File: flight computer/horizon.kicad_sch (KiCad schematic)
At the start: 44 parts, among them J2 Conn_02x03_Counter_Clockwise, J7 Conn_02x03_Counter_Clockwise, J8 Conn_02x03_Counter_Clockwise, SW1 CK_KMS2xxG, U1 MMCU, U2 MKL02Z32VFG4, Y1 32 kHZ

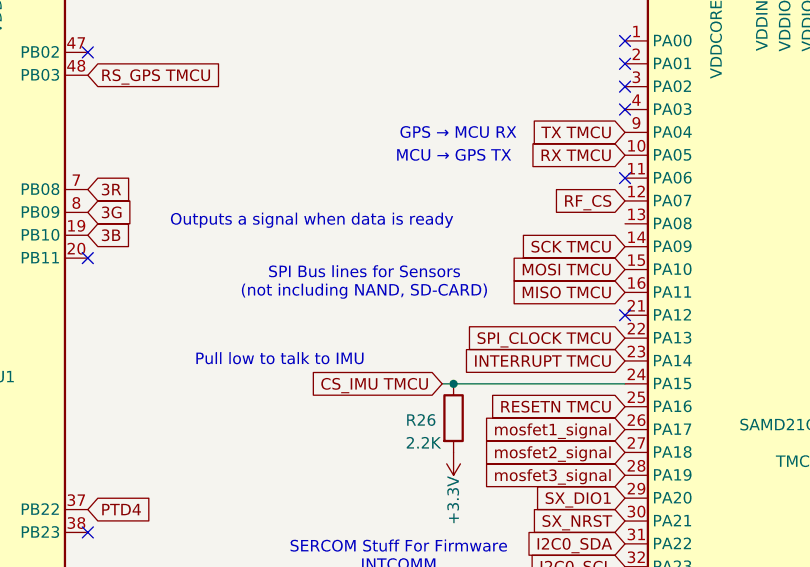
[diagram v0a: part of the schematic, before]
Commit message: swap spi lines on tmcu
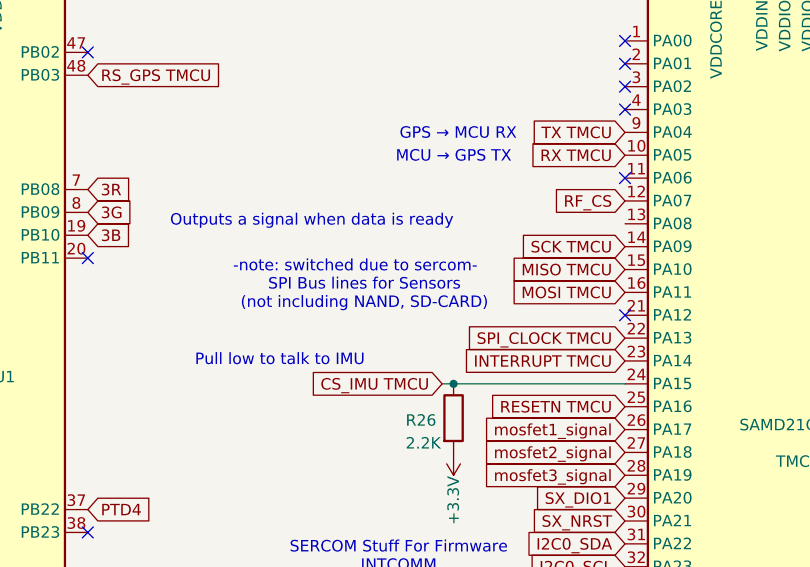
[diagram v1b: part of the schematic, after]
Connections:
- net MISO TMCU: now also SAMD21G18A-AU2.15 (PA10); no longer SAMD21G18A-AU2.16 (PA11)
- net MOSI TMCU: now also SAMD21G18A-AU2.16 (PA11); no longer SAMD21G18A-AU2.15 (PA10)
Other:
- note added: "-note: switched due to sercom-"
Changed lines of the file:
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@@
+		)
+	)
+	(text "-note: switched due to sercom-"
+		(exclude_from_sim no)
+		(at 97.028 69.596 0)
+		(effects
+			(font
+				(size 1.27 1.27)
+			)
 		)
 	)
@@
 	(text "SPI Bus lines for Sensors \n(not including NAND, SD-CARD)"
 		(exclude_from_sim no)
-		(at 98.044 71.374 0)
+		(at 98.044 72.644 0)
 		(effects
 			(font
@@
 	(global_label "MOSI TMCU"
 		(shape input)
+		(at 127 72.39 180)
+		(fields_autoplaced yes)
+		(effects
+			(font
+				(size 1.27 1.27)
+			)
+			(justify right)
+		)
+		(property "Intersheetrefs" "${INTERSHEET_REFS}"
+			(at 113.4315 72.39 0)
+			(effects
+				(font
+					(size 1.27 1.27)
+				)
+				(justify right)
+				(hide yes)
+			)
+		)
+	)
+	(global_label "CAM_TX"
+		(shape input)
+		(at 232.41 30.48 180)
+		(fields_autoplaced yes)
+		(effects
+			(font
+				(size 1.27 1.27)
+			)
+			(justify right)
+		)
+		(property "Intersheetrefs" "${INTERSHEET_REFS}"
+			(at 222.4701 30.48 0)
+			(effects
+				(font
+					(size 1.27 1.27)
+				)
+				(justify right)
+				(hide yes)
+			)
+		)
+	)
+	(global_label "2G"
+		(shape input)
+		(at 162.56 67.31 0)
+		(fields_autoplaced yes)
+		(effects
+			(font
+				(size 1.27 1.27)
+			)
+			(justify left)
+		)
+		(property "Intersheetrefs" "${INTERSHEET_REFS}"
+			(at 168.0247 67.31 0)
+			(effects
+				(font
+					(size 1.27 1.27)
+				)
+				(justify left)
+				(hide yes)
+			)
+		)
+	)
+	(global_label "SCK TMCU"
+		(shape input)
+		(at 127 67.31 180)
+		(fields_autoplaced yes)
+		(effects
+			(font
+				(size 1.27 1.27)
+			)
+			(justify right)
+		)
+		(property "Intersheetrefs" "${INTERSHEET_REFS}"
+			(at 114.2782 67.31 0)
+			(effects
+				(font
+					(size 1.27 1.27)
+				)
+				(justify right)
+				(hide yes)
+			)
+		)
+	)
+	(global_label "D+ DMCU-2"
+		(shape input)
+		(at 118.11 107.95 180)
+		(fields_autoplaced yes)
+		(effects
+			(font
+				(size 1.27 1.27)
+			)
+			(justify right)
+		)
+		(property "Intersheetrefs" "${INTERSHEET_REFS}"
+			(at 103.211 107.95 0)
+			(effects
+				(font
+					(size 1.27 1.27)
+				)
+				(justify right)
+				(hide yes)
+			)
+		)
+	)
+	(global_label "TX TMCU"
+		(shape input)
+		(at 127 54.61 180)
+		(fields_autoplaced yes)
+		(effects
+			(font
+				(size 1.27 1.27)
+			)
+			(justify right)
+		)
+		(property "Intersheetrefs" "${INTERSHEET_REFS}"
+			(at 115.8506 54.61 0)
+			(effects
+				(font
+					(size 1.27 1.27)
+				)
+				(justify right)
+				(hide yes)
+			)
+		)
+	)
+	(global_label "PTA2"
+		(shape input)
+		(at 290.83 106.68 0)
+		(fields_autoplaced yes)
+		(effects
+			(font
+				(size 1.27 1.27)
+			)
+			(justify left)
+		)
+		(property "Intersheetrefs" "${INTERSHEET_REFS}"
+			(at 298.3509 106.68 0)
+			(effects
+				(font
+					(size 1.27 1.27)
+				)
+				(justify left)
+				(hide yes)
+			)
+		)
+	)
+	(global_label "MISO TMCU"
+		(shape input)
 		(at 127 69.85 180)
 		(fields_autoplaced yes)
@@
 			(effects
 				(font
-					(size 1.27 1.27)
-				)
-				(justify right)
-				(hide yes)
-			)
-		)
-	)
-	(global_label "CAM_TX"
-		(shape input)
-		(at 232.41 30.48 180)
-		(fields_autoplaced yes)
-		(effects
-			(font
-				(size 1.27 1.27)
-			)
-			(justify right)
-		)
-		(property "Intersheetrefs" "${INTERSHEET_REFS}"
-			(at 222.4701 30.48 0)
-			(effects
-				(font
-					(size 1.27 1.27)
-				)
-				(justify right)
-				(hide yes)
-			)
-		)
-	)
-	(global_label "2G"
-		(shape input)
-		(at 162.56 67.31 0)
-		(fields_autoplaced yes)
-		(effects
-			(font
-				(size 1.27 1.27)
-			)
-			(justify left)
-		)
-		(property "Intersheetrefs" "${INTERSHEET_REFS}"
-			(at 168.0247 67.31 0)
-			(effects
-				(font
-					(size 1.27 1.27)
-				)
-				(justify left)
-				(hide yes)
-			)
-		)
-	)
-	(global_label "SCK TMCU"
-		(shape input)
-		(at 127 67.31 180)
-		(fields_autoplaced yes)
-		(effects
-			(font
-				(size 1.27 1.27)
-			)
-			(justify right)
-		)
-		(property "Intersheetrefs" "${INTERSHEET_REFS}"
-			(at 114.2782 67.31 0)
-			(effects
-				(font
-					(size 1.27 1.27)
-				)
-				(justify right)
-				(hide yes)
-			)
-		)
-	)
-	(global_label "D+ DMCU-2"
-		(shape input)
-		(at 118.11 107.95 180)
-		(fields_autoplaced yes)
-		(effects
-			(font
-				(size 1.27 1.27)
-			)
-			(justify right)
-		)
-		(property "Intersheetrefs" "${INTERSHEET_REFS}"
-			(at 103.211 107.95 0)
-			(effects
-				(font
-					(size 1.27 1.27)
-				)
-				(justify right)
-				(hide yes)
-			)
-		)
-	)
-	(global_label "TX TMCU"
-		(shape input)
-		(at 127 54.61 180)
-		(fields_autoplaced yes)
-		(effects
-			(font
-				(size 1.27 1.27)
-			)
-			(justify right)
-		)
-		(property "Intersheetrefs" "${INTERSHEET_REFS}"
-			(at 115.8506 54.61 0)
-			(effects
-				(font
-					(size 1.27 1.27)
-				)
-				(justify right)
-				(hide yes)
-			)
-		)
-	)
-	(global_label "PTA2"
-		(shape input)
-		(at 290.83 106.68 0)
-		(fields_autoplaced yes)
-		(effects
-			(font
-				(size 1.27 1.27)
-			)
-			(justify left)
-		)
-		(property "Intersheetrefs" "${INTERSHEET_REFS}"
-			(at 298.3509 106.68 0)
-			(effects
-				(font
-					(size 1.27 1.27)
-				)
-				(justify left)
-				(hide yes)
-			)
-		)
-	)
-	(global_label "MISO TMCU"
-		(shape input)
-		(at 127 72.39 180)
-		(fields_autoplaced yes)
-		(effects
-			(font
-				(size 1.27 1.27)
-			)
-			(justify right)
-		)
-		(property "Intersheetrefs" "${INTERSHEET_REFS}"
-			(at 113.4315 72.39 0)
-			(effects
-				(font

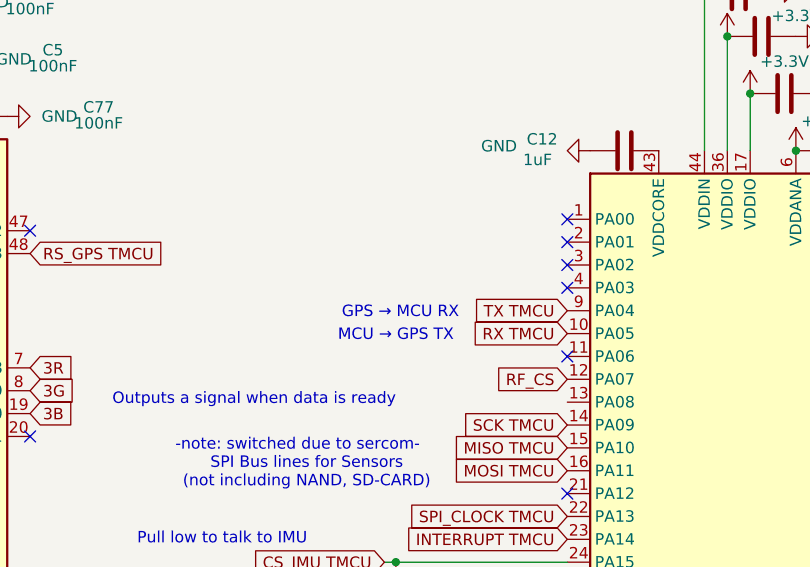
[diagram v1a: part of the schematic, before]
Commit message: note: referenced to vddana
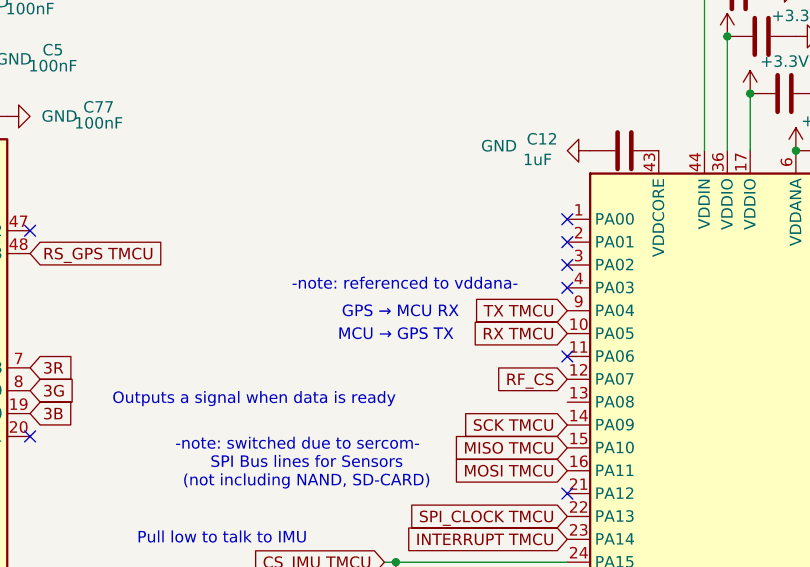
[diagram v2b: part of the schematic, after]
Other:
- note added: "-note: referenced to vddana-"
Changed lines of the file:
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@@
+		)
+	)
+	(text "-note: referenced to vddana-"
+		(exclude_from_sim no)
+		(at 108.966 51.816 0)
+		(effects
+			(font
+				(size 1.27 1.27)
+			)
 		)
 	)

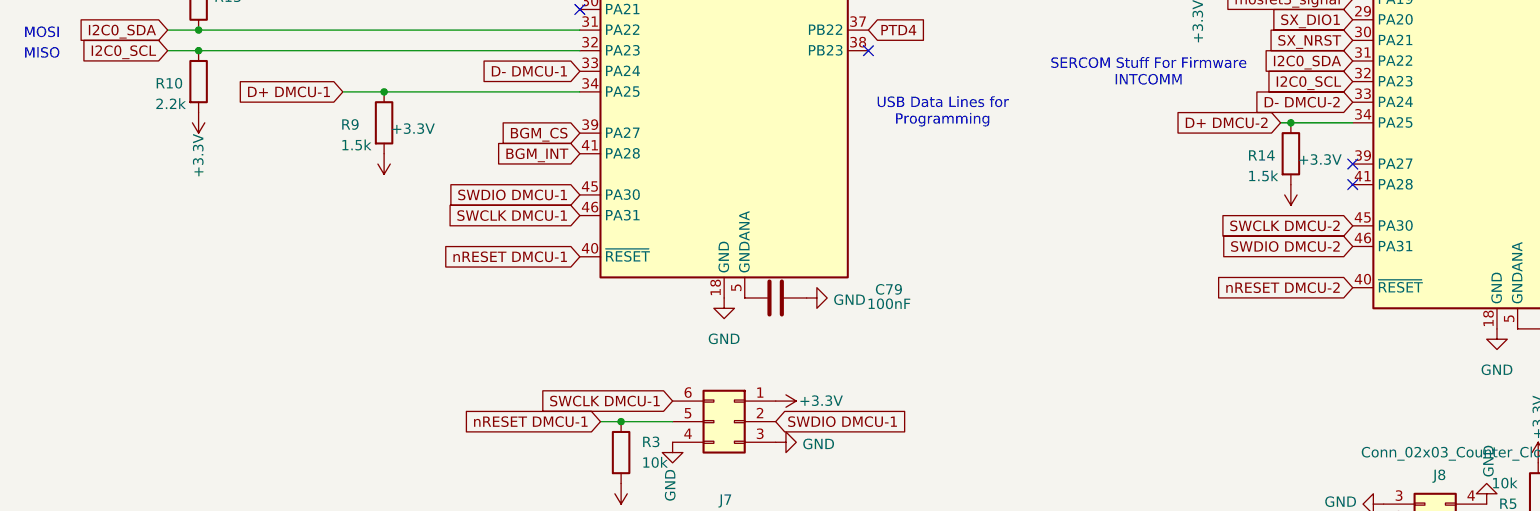
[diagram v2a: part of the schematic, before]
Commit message: swapping swd on nmcu
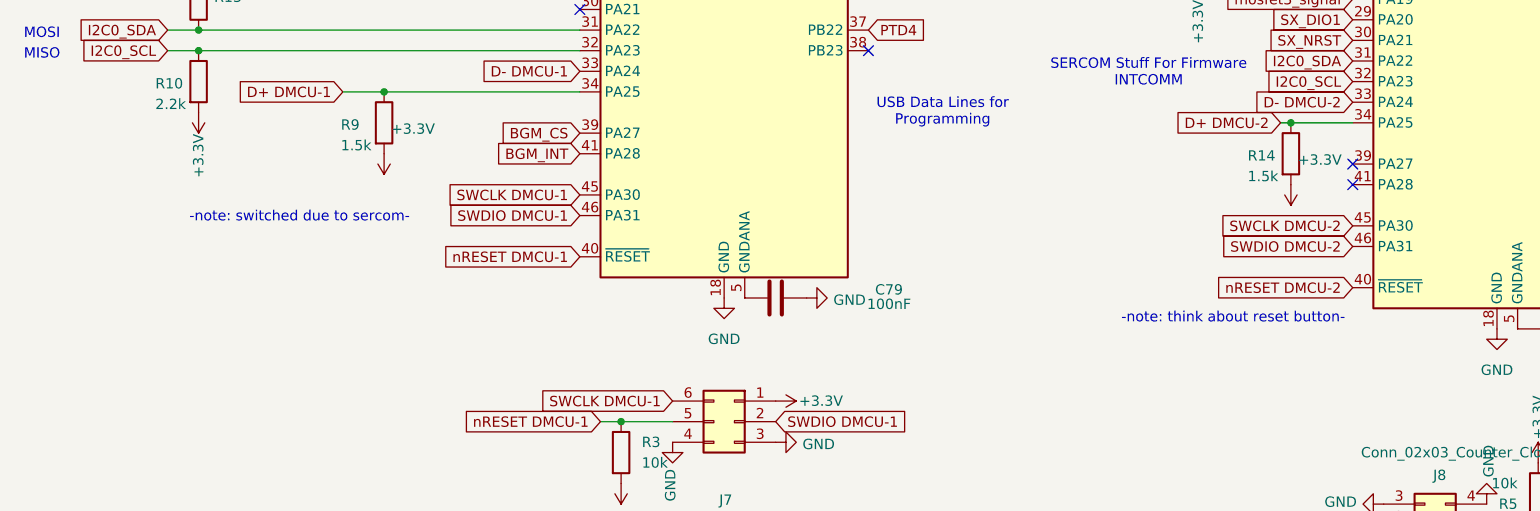
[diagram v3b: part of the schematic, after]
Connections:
- net SWCLK DMCU-1: now also SAMD21G18A-AU1.45 (PA30); no longer SAMD21G18A-AU1.46 (PA31)
- net SWDIO DMCU-1: now also SAMD21G18A-AU1.46 (PA31); no longer SAMD21G18A-AU1.45 (PA30)
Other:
- note added: "-note: think about reset button-"

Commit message: samds look good to me
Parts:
- removed C78, C79: 100nF, Capacitor_SMD:C_0603_1608Metric, symbol Device:C
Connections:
- net GND: now also SAMD21G18A-AU1.5 (GNDANA), SAMD21G18A-AU2.5 (GNDANA)
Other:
- note added: "-note: direct to gnd-"
- note removed: "-note: referenced to vddana-"
- note removed: "MISO"
- note removed: "MOSI"

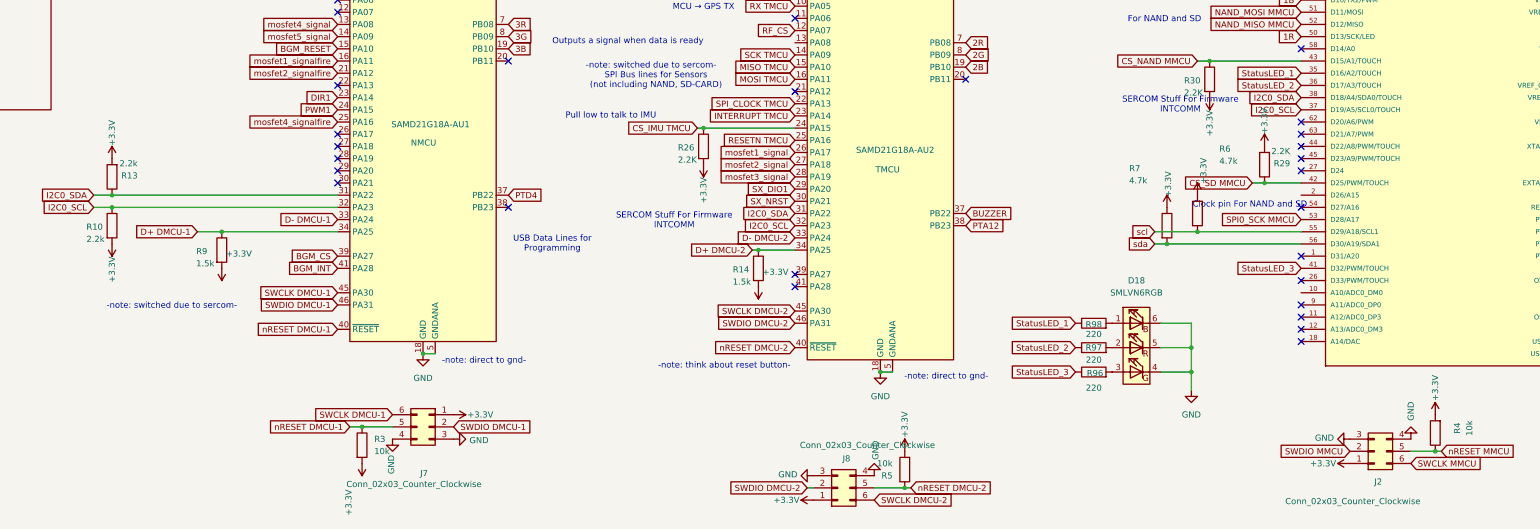
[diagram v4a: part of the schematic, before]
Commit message: fixed micro sd card direction and prod files
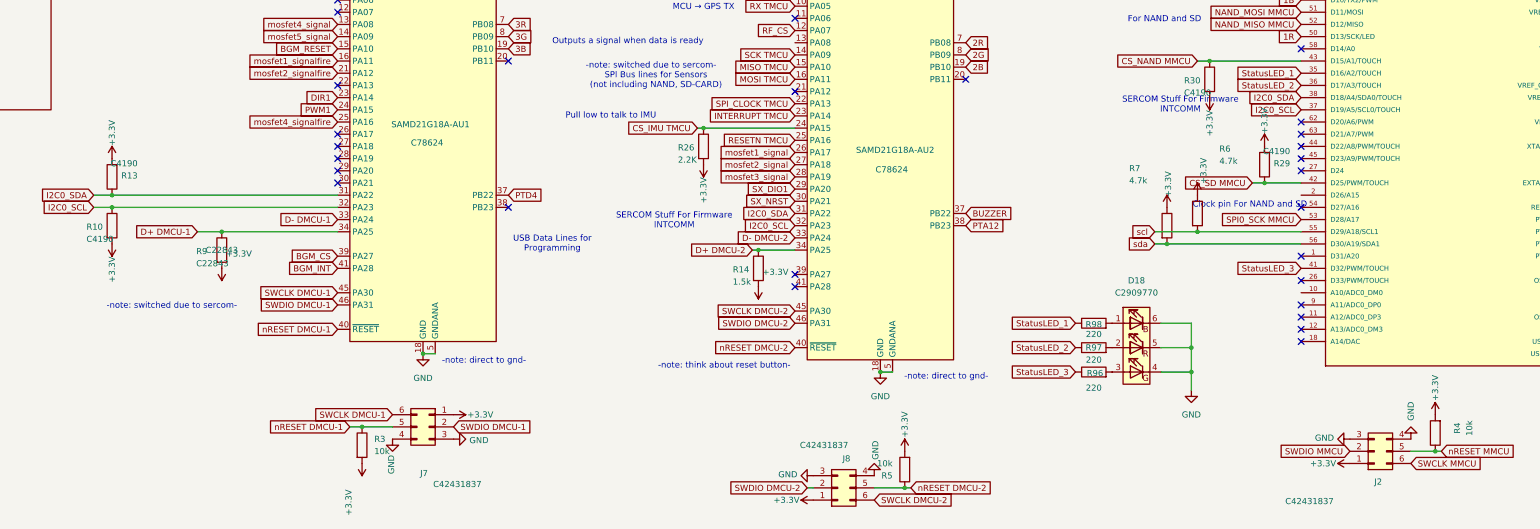
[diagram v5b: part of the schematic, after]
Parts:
- D18: value SMLVN6RGB -> C2909770
- J2, J7, J8: value Conn_02x03_Counter_Clockwise -> C42431837
- R10, R13: value 2.2k -> C4190
- R29, R30: value 2.2K -> C4190
- R9: value 1.5k -> C22843; LCSC (none) -> C22843
- SAMD21G18A-AU1: value NMCU -> C78624
- SAMD21G18A-AU2: value TMCU -> C78624
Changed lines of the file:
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@@
 			)
 		)
-		(property "Value" "2.2k"
+		(property "Value" "C4190"
 			(at -9.906 89.916 0)
 			(effects
@@
 			)
 		)
-		(property "Value" "Conn_02x03_Counter_Clockwise"
+		(property "Value" "C42431837"
 			(at 128.016 148.59 0)
 			(effects
@@
 			)
 		)
-		(property "Value" "Conn_02x03_Counter_Clockwise"
+		(property "Value" "C42431837"
 			(at 61.722 156.718 0)
 			(effects
@@
 			)
 		)
-		(property "Value" "Conn_02x03_Counter_Clockwise"
+		(property "Value" "C42431837"
 			(at 229.108 160.274 0)
 			(effects
@@
 			)
 		)
-		(property "Value" "TMCU"
+		(property "Value" "C78624"
 			(at 143.764 91.186 0)
 			(effects
@@
 			)
 		)
-		(property "Value" "2.2k"
+		(property "Value" "C4190"
 			(at -20.574 105.664 0)
 			(effects
@@
 			)
 		)
-		(property "Value" "2.2K"
+		(property "Value" "C4190"
 			(at 208.026 75.184 0)
 			(effects
@@
 			)
 		)
-		(property "Value" "NMCU"
+		(property "Value" "C78624"
 			(at 46.99 85.598 0)
 			(effects
@@
 			)
 		)
-		(property "Value" "2.2K"
+		(property "Value" "C4190"
 			(at 230.124 87.376 0)
 			(effects
@@
 			)
 		)
-		(property "Value" "SMLVN6RGB"
+		(property "Value" "C2909770"
 			(at 198.12 116.84 0)
 			(effects
@@
 			)
 		)
-		(property "Value" "1.5k"
+		(property "Value" "C22843"
 			(at 2.286 110.744 0)
 			(effects
@@
 			)
 		)
-		(property "Description" "Resistor"
+		(property "Description" "C22843"
 			(at 7.62 107.95 0)
 			(effects
@@
 			)
 		)
+		(property "LCSC" "C22843"
+			(at 7.62 107.95 0)
+			(effects
+				(font
+					(size 1.27 1.27)
+				)
+			)
+		)

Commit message: fixed crystal
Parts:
- C10, C17: value 12pF -> 12.5pF
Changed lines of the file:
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@@
 			)
 		)
-		(property "Value" "12pF"
+		(property "Value" "12.5pF"
 			(at 309.372 91.186 90)
 			(effects
@@
 			)
 		)
-		(property "Value" "12pF"
+		(property "Value" "12.5pF"
 			(at 304.038 91.694 90)
 			(effects
